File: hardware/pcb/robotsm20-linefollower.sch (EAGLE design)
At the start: 101 parts, among them IC1 BNO055, IC2 TPS43061RTER, Q1 CSD15571Q2, Q2 CSD15571Q2, U1 STM32F405RG

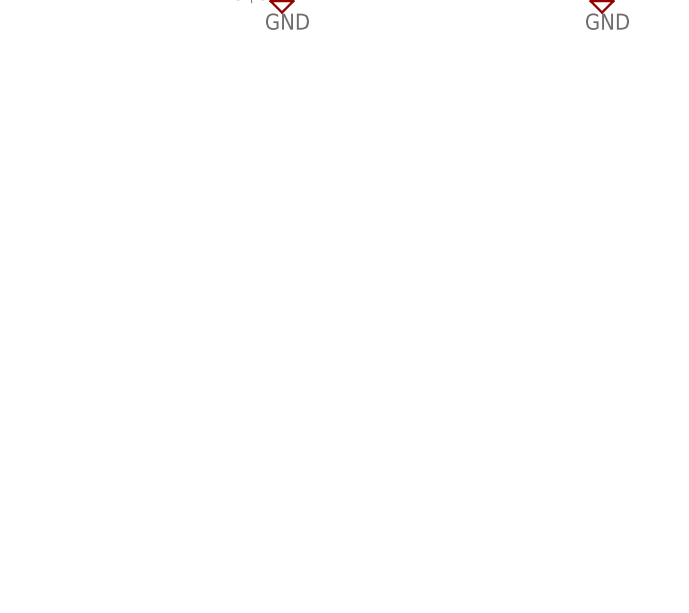
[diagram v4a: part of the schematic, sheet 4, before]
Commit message: Added interface button
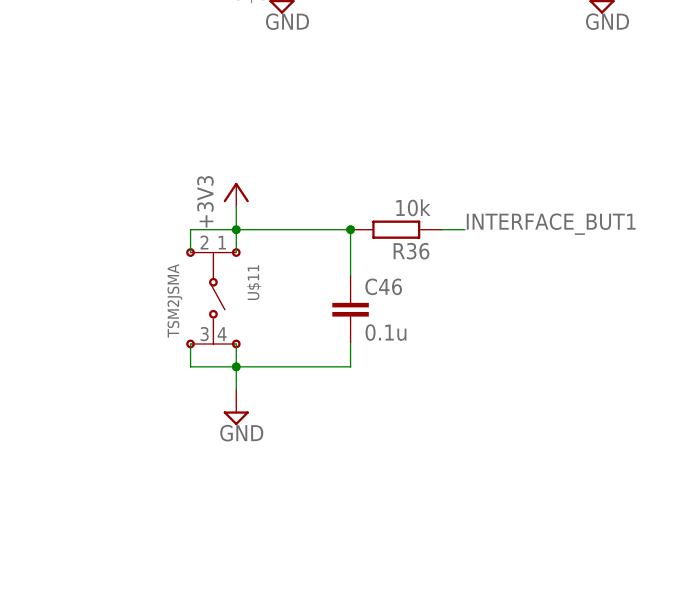
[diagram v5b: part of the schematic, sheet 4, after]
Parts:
- added C46: 0.1u, rcl:C-EUC0805
- added R36: 10k, rcl:R-EU_R0603
- added U$11: TSM2JSMA, CASE-Switches:TSM2JSMA
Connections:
- new net INTERFACE_BUT1: R36.1
- net +3V3: now also C46.1, R36.2, U$11.1, U$11.2
- net GND: now also C46.2, U$11.3, U$11.4
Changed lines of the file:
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@@
 <schematic_group name="IMU"/>
 <schematic_group name="BATTERY"/>
+<schematic_group name="INTERFACE-BUTTON"/>
 </groups>
 <parts>
@@
 <part name="R32" library="rcl" library_urn="urn:adsk.eagle:library:334" deviceset="R-EU_" device="R0603" package3d_urn="urn:adsk.eagle:package:23555/3" value="10k"/>
 <part name="R35" library="rcl" library_urn="urn:adsk.eagle:library:334" deviceset="R-EU_" device="R0603" package3d_urn="urn:adsk.eagle:package:23555/3" value="10k"/>
+<part name="U$11" library="CASE-Switches" library_urn="urn:adsk.eagle:library:7770839" deviceset="TSM2JSMA" device="" package3d_urn="urn:adsk.eagle:package:17798453/2"/>
+<part name="C46" library="rcl" library_urn="urn:adsk.eagle:library:334" deviceset="C-EU" device="C0805" package3d_urn="urn:adsk.eagle:package:23617/2" value="0.1u"/>
+<part name="SUPPLY70" library="supply2" library_urn="urn:adsk.eagle:library:372" deviceset="GND" device=""/>
+<part name="+3V6" library="supply1" library_urn="urn:adsk.eagle:library:371" deviceset="+3V3" device=""/>
+<part name="R36" library="rcl" library_urn="urn:adsk.eagle:library:334" deviceset="R-EU_" device="R0603" package3d_urn="urn:adsk.eagle:package:23555/3" value="10k"/>
 </parts>
 <sheets>
@@
 <attribute name="VALUE" x="178.562" y="49.53" size="1.778" layer="96" rot="R90"/>
 </instance>
+<instance part="U$11" gate="G$1" x="134.62" y="0" smashed="yes" rot="R270" grouprefs="INTERFACE-BUTTON">
+<attribute name="NAME" x="135.89" y="-3.81" size="1.27" layer="95" ratio="10" rot="R270"/>
+<attribute name="VALUE" x="127" y="-3.81" size="1.27" layer="95" ratio="10" rot="R270"/>
+</instance>
+<instance part="C46" gate="G$1" x="147.32" y="-7.62" smashed="yes" grouprefs="INTERFACE-BUTTON">
+<attribute name="NAME" x="148.844" y="-7.239" size="1.778" layer="95"/>
+<attribute name="VALUE" x="148.844" y="-12.319" size="1.778" layer="96"/>
+</instance>
+<instance part="SUPPLY70" gate="GND" x="134.62" y="-20.32" smashed="yes" grouprefs="INTERFACE-BUTTON">
+<attribute name="VALUE" x="132.715" y="-23.495" size="1.778" layer="96"/>
+</instance>
+<instance part="+3V6" gate="G$1" x="134.62" y="5.08" smashed="yes" grouprefs="INTERFACE-BUTTON">
+<attribute name="VALUE" x="132.08" y="0" size="1.778" layer="96" rot="R90"/>
+</instance>
+<instance part="R36" gate="G$1" x="152.4" y="0" smashed="yes" rot="R180" grouprefs="INTERFACE-BUTTON">
+<attribute name="NAME" x="156.21" y="-1.4986" size="1.778" layer="95" rot="R180"/>
+<attribute name="VALUE" x="156.21" y="3.302" size="1.778" layer="96" rot="R180"/>
+</instance>
 </instances>
 <busses>
@@
 <wire x1="175.26" y1="27.94" x2="175.26" y2="38.1" width="0.1524" layer="91" grouprefs="BATTERY"/>
 <wire x1="175.26" y1="38.1" x2="170.18" y2="38.1" width="0.1524" layer="91" grouprefs="BATTERY"/>
+</segment>
+<segment>
+<pinref part="C46" gate="G$1" pin="2"/>
+<wire x1="147.32" y1="-12.7" x2="147.32" y2="-15.24" width="0.1524" layer="91" grouprefs="INTERFACE-BUTTON"/>
+<pinref part="U$11" gate="G$1" pin="3"/>
+<wire x1="129.54" y1="-12.7" x2="129.54" y2="-15.24" width="0.1524" layer="91" grouprefs="INTERFACE-BUTTON"/>
+<wire x1="129.54" y1="-15.24" x2="134.62" y2="-15.24" width="0.1524" layer="91" grouprefs="INTERFACE-BUTTON"/>
+<pinref part="U$11" gate="G$1" pin="4"/>
+<wire x1="134.62" y1="-15.24" x2="134.62" y2="-12.7" width="0.1524" layer="91" grouprefs="INTERFACE-BUTTON"/>
+<wire x1="134.62" y1="-15.24" x2="147.32" y2="-15.24" width="0.1524" layer="91" grouprefs="INTERFACE-BUTTON"/>
+<junction x="134.62" y="-15.24" grouprefs="INTERFACE-BUTTON"/>
+<pinref part="SUPPLY70" gate="GND" pin="GND"/>
+<wire x1="134.62" y1="-17.78" x2="134.62" y2="-15.24" width="0.1524" layer="91" grouprefs="INTERFACE-BUTTON"/>
 </segment>
 </net>
@@
 <pinref part="R29" gate="G$1" pin="2"/>
 <pinref part="+3V4" gate="G$1" pin="+3V3"/>
+</segment>
+<segment>
+<pinref part="U$11" gate="G$1" pin="2"/>
+<wire x1="129.54" y1="-2.54" x2="129.54" y2="0" width="0.1524" layer="91" grouprefs="INTERFACE-BUTTON"/>
+<wire x1="129.54" y1="0" x2="134.62" y2="0" width="0.1524" layer="91" grouprefs="INTERFACE-BUTTON"/>
+<pinref part="U$11" gate="G$1" pin="1"/>
+<wire x1="134.62" y1="0" x2="134.62" y2="-2.54" width="0.1524" layer="91" grouprefs="INTERFACE-BUTTON"/>
+<pinref part="+3V6" gate="G$1" pin="+3V3"/>
+<wire x1="134.62" y1="0" x2="134.62" y2="2.54" width="0.1524" layer="91" grouprefs="INTERFACE-BUTTON"/>
+<junction x="134.62" y="0" grouprefs="INTERFACE-BUTTON"/>
+<wire x1="134.62" y1="0" x2="147.32" y2="0" width="0.1524" layer="91" grouprefs="INTERFACE-BUTTON"/>
+<pinref part="C46" gate="G$1" pin="1"/>
+<wire x1="147.32" y1="-5.08" x2="147.32" y2="0" width="0.1524" layer="91" grouprefs="INTERFACE-BUTTON"/>
+<pinref part="R36" gate="G$1" pin="2"/>
+<junction x="147.32" y="0"/>
 </segment>
 </net>
@@
 </segment>
 </net>
+<net name="INTERFACE_BUT1" class="0">
+<segment>
+<pinref part="R36" gate="G$1" pin="1"/>
+<wire x1="157.48" y1="0" x2="160.02" y2="0" width="0.1524" layer="91" grouprefs="INTERFACE-BUTTON"/>
+<label x="160.02" y="0" size="1.778" layer="95" grouprefs="INTERFACE-BUTTON"/>
+</segment>
+</net>

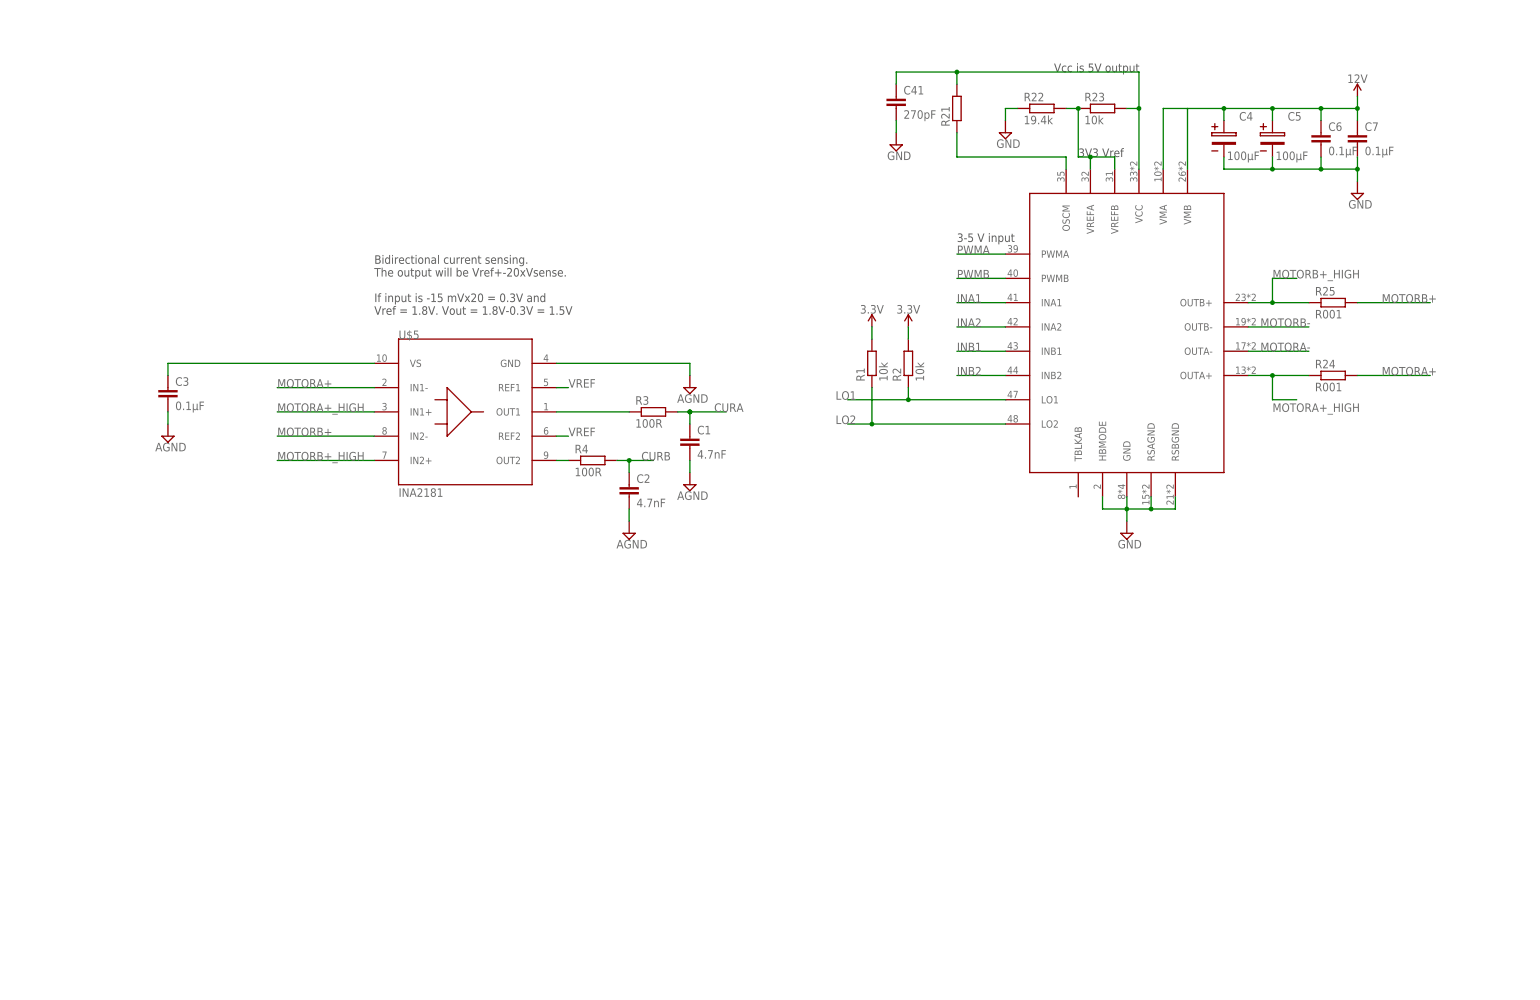
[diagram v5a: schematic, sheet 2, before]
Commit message: Added rgb led, xt30 for battery and changed to nmosfet
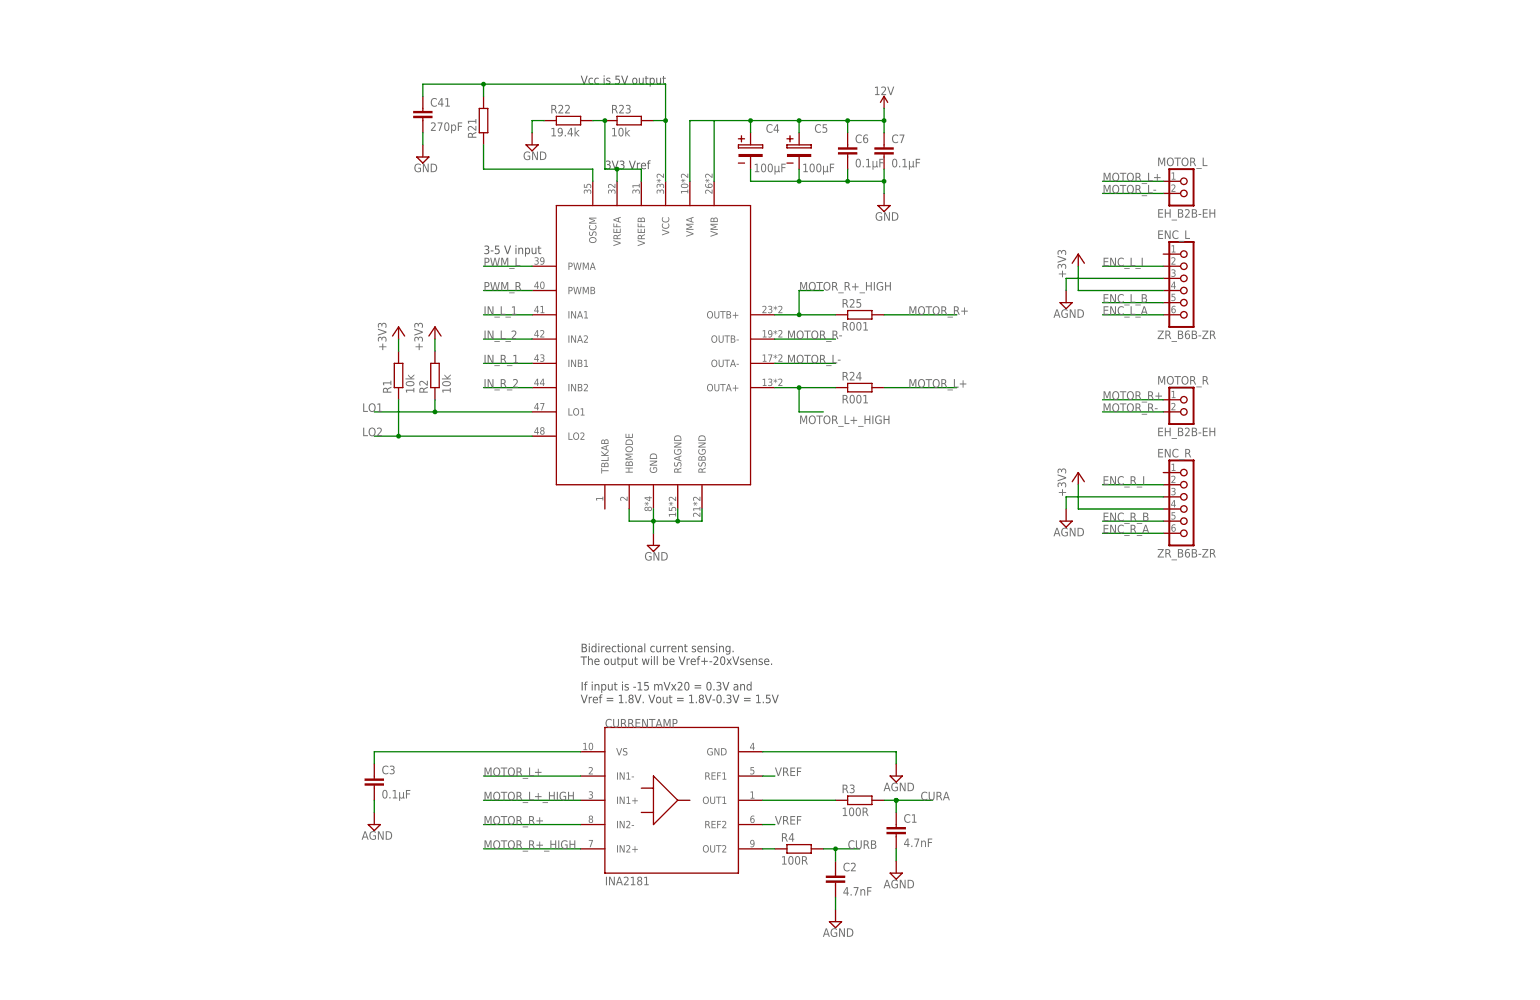
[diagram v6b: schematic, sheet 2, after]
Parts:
- removed U$1: TB67H420FTG, MotorDriver:TB67H420FTG
- removed U$10: DMP2010UFV, PowerManagement:DMP2010UFV
- removed U$5: INA2181, MotorDriver:INA2181
- removed U$8: JS202011AQN, Switches:JS202011AQN
- removed U$9: JST-XH-03, Isaks Bibliotek:JST-XH-03
- added CURRENTAMP: INA2181, MotorDriver:INA2181
- added D1: CHIP-LED0805, CASE-LED:CHIP-LED0805
- added ENC_L, ENC_R: ZR_B6B-ZR, CASE-JST:ZR_B6B-ZR
- added LED1: 150141M173100, CASE-LED:150141M173100
- added MOTORDRIVER: TB67H420FTG, MotorDriver:TB67H420FTG
- added MOTOR_L, MOTOR_R: EH_B2B-EH, CASE-JST:EH_B2B-EH
- added Q3, Q4: CSD15571Q2, PowerManagement:CSD15571Q2
- added Q5, Q6, Q7: BSS138LT3G, CASE-Transistors:BSS138LT3G
- added R37: 100R, rcl:R-EU_R0603
- added R38, R40: 0R, rcl:R-EU_R0603
- added R39, R41, R42: 10k, rcl:R-EU_R0603
- added U$15: XT30PW-M, Connectors:XT30PW-M
- added U$16: JS202011AQN, Switches:JS202011AQN
- R32: value 10k -> 245R
- R36: value 10k -> 50R
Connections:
- removed net INA1: U$1.INA1
- removed net INA2: U$1.INA2
- removed net INB1: U$1.INB1
- removed net INB2: U$1.INB2
- removed net MOTORA+: R24.2, U$5.IN1-
- removed net MOTORA+_HIGH: R24.1, U$1.OUTA+, U$5.IN1+
- removed net MOTORA-: U$1.OUTA-
- removed net MOTORB+: R25.2, U$5.IN2-
- removed net MOTORB+_HIGH: R25.1, U$1.OUTB+, U$5.IN2+
- removed net MOTORB-: U$1.OUTB-
- removed net N$60: U1.PB7
- removed net N$62: U1.PB5
- removed net N$63: U1.PB6
- removed net N$65: U1.PB4
- removed net PWMA: U$1.PWMA
- removed net PWMB: U$1.PWMB
- new net 3.3V1: R41.1, R42.1
- new net BAT-: Q3.S, Q4.S, R39.1, U$15.-, U$16.NC
- new net ENC_L_I: ENC_L.2
- new net ENC_R_I: ENC_R.2
- new net IN_L_1: MOTORDRIVER.INA1, U1.PB4
- new net IN_L_2: MOTORDRIVER.INA2, U1.PB5
- new net IN_R_1: MOTORDRIVER.INB1, U1.PB6
- new net IN_R_2: MOTORDRIVER.INB2, U1.PB7
- new net MOTOR_L+: CURRENTAMP.IN1-, MOTOR_L.1, R24.2
- new net MOTOR_L+_HIGH: CURRENTAMP.IN1+, MOTORDRIVER.OUTA+, R24.1
- new net MOTOR_L-: MOTORDRIVER.OUTA-, MOTOR_L.2
- new net MOTOR_R+: CURRENTAMP.IN2-, MOTOR_R.1, R25.2
- new net MOTOR_R+_HIGH: CURRENTAMP.IN2+, MOTORDRIVER.OUTB+, R25.1
- new net MOTOR_R-: MOTORDRIVER.OUTB-, MOTOR_R.2
- new net N$41: Q3.G, Q4.G, R37.1
- new net N$43: LED1.B, R40.2
- new net N$45: Q5.D, R36.1
- new net N$46: Q6.D, R38.1
- new net N$47: R37.2, R39.2, U$16.COM
- new net N$48: Q7.D, R40.1
- net +3V3: now also ENC_L.4, ENC_R.4, LED1.CA, R1.2, R2.2, R35.2; no longer C46.1, R36.2
- net 12V: now also MOTORDRIVER.VMA; no longer U$1.VMA
- net 3.3V: no longer R1.2, R2.2
- net AGND: now also CURRENTAMP.GND, ENC_L.3, ENC_R.3; no longer U$5.GND
- net ENC_L_A: now also ENC_L.6
- net ENC_L_B: now also ENC_L.5
- net ENC_R_A: now also ENC_R.6
- net ENC_R_B: now also ENC_R.5
- net GND: now also MOTORDRIVER.GND, MOTORDRIVER.HBMODE, MOTORDRIVER.RSAGND, MOTORDRIVER.RSBGND, Q3.D, Q4.D, Q5.S, Q6.S, Q7.S, R32.1; no longer U$1.GND, U$1.HBMODE, U$1.RSAGND, U$1.RSBGND, U$8.NO, U$9.1
- net INTERFACE_BUT1: now also C46.1, R35.1; no longer R36.1
- net LED_B: now also Q7.G
- net LED_G: now also Q6.G
- net LED_R: now also Q5.G
- net LO1: now also MOTORDRIVER.LO1; no longer U$1.LO1
- net LO2: now also MOTORDRIVER.LO2; no longer U$1.LO2
- net N$2: now also MOTORDRIVER.VMB; no longer U$1.VMB
- net N$28: now also MOTORDRIVER.VREFA, MOTORDRIVER.VREFB; no longer U$1.VREFA, U$1.VREFB
- net N$29: now also MOTORDRIVER.VCC; no longer U$1.VCC
- net N$31: now also MOTORDRIVER.OSCM; no longer U$1.OSCM
- net N$38: now also D1.K, R32.2; no longer U$10.S, U$9.3
- net N$40: now also LED1.R, R36.2; no longer R32.1, U$10.G, U$8.COM
- net N$42: now also LED1.G, R38.2; no longer R35.1, U$8.NC
- net N$7: now also CURRENTAMP.OUT2; no longer U$5.OUT2
- net N$8: now also CURRENTAMP.OUT1; no longer U$5.OUT1
- net N$9: now also CURRENTAMP.VS; no longer U$5.VS
- net PWM_L: now also MOTORDRIVER.PWMA
- net PWM_R: now also MOTORDRIVER.PWMB
- net RX: now also R41.2
- net TX: now also R42.2
- net V+: now also D1.A, U$15.+, U$16.NO; no longer R32.2, R35.2, U$10.D
- net VREF: now also CURRENTAMP.REF1, CURRENTAMP.REF2; no longer U$5.REF1, U$5.REF2
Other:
- note added: "Don't know if internal is too weak"
- note added: "Don't know if there is internal pullup or in the I2C display"
- note added: "Dual N-channel mosfet for connect/disconnect the battery. A LED to show when battery is connected and switch is on."
- note added: "Red 20mA 2V Green 20mA 3.2V Blue 20mA 3.2V Utilizing internal pull-down"
- note removed: "OFF"
- note removed: "ON"
- moved on the sheet: C1, C2, C3, C4, C41, C46, C5, C6, C7, R1, R2, R21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
